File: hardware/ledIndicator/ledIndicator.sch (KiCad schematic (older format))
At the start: 12 parts

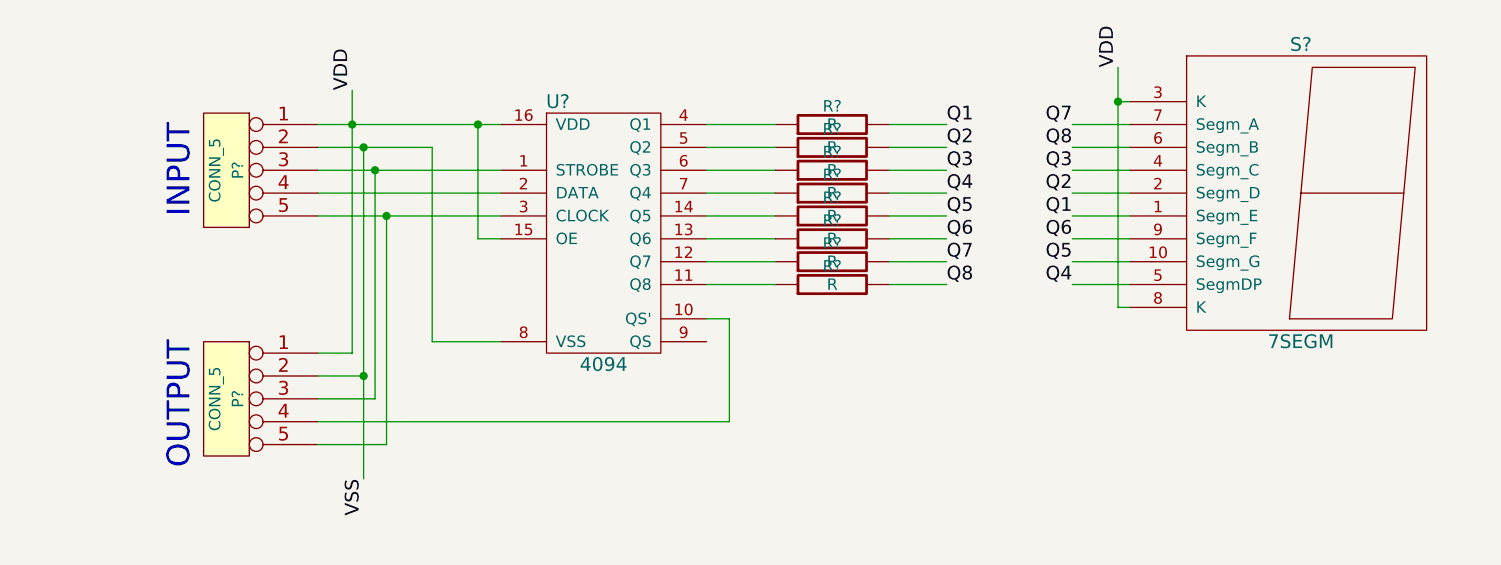
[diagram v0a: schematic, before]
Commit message: Initial design of the layout on pcb
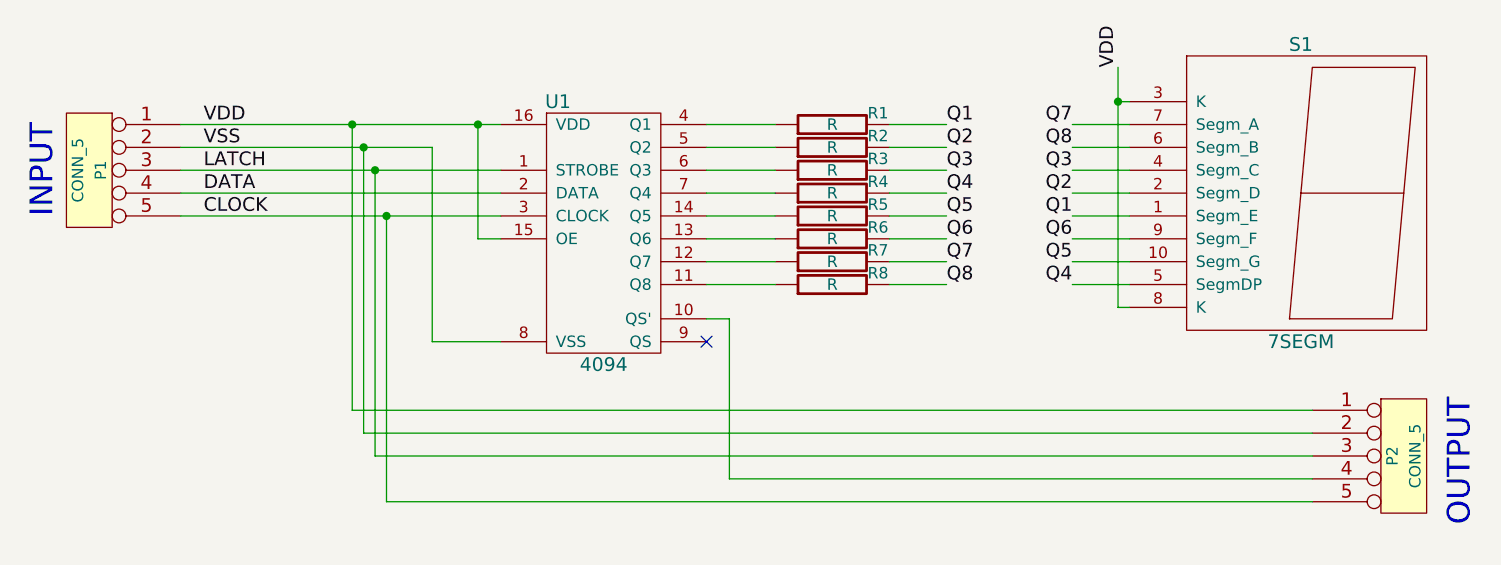
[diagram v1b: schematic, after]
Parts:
- P1, P2: renamed from P?; footprint (none) -> SMD_CONN5
- R1, R2, R3, R4, R5, R6, R7, R8: renamed from R?; footprint (none) -> SM0603_Resistor
- S1: renamed from S?; footprint (none) -> SA56
- U1: renamed from U?; footprint (none) -> SO16N
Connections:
- net LATCH: now reaches P1.3, P2.3, U1.1 (STROBE)
- net DATA: now reaches P1.4, U1.2 (DATA)
- net CLOCK: now reaches P1.5, P2.5, U1.3 (CLOCK)
- no-connect marks 0 -> 1
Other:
- moved on the sheet: P1, P2
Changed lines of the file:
@@
-EESchema Schematic File Version 2  date  3.01.2013 (чт)  1,24,30 EET
+EESchema Schematic File Version 2  date Thu 03 Jan 2013 05:14:04 PM EET
 LIBS:power
 LIBS:device
@@
 LIBS:contrib
 LIBS:valves
+LIBS:ledIndicator-cache
 EELAYER 27 0
 EELAYER END
@@
 Sheet 1 1
 Title "7 SEGMENT LED DISPLAY FOR PIPO"
-Date "2 jan 2013"
+Date "3 jan 2013"
 Rev "rev.A"
 Comp ""
@@
 $EndDescr
 $Comp
-L 7SEGM S?
+L 7SEGM S1
 U 1 1 50E4B02C
 P 7950 3450
-F 0 "S?" H 7950 4100 60  0000 C CNN
+F 0 "S1" H 7950 4100 60  0000 C CNN
 F 1 "7SEGM" H 7950 2800 60  0000 C CNN
+F 2 "SA56" H 7950 3450 60  0001 C CNN
 	1    7950 3450
 	1    0    0    -1
 $EndComp
 $Comp
-L 4094 U?
+L 4094 U1
 U 1 1 50E4C062
 P 4900 3700
-F 0 "U?" H 4700 4350 60  0000 C CNN
+F 0 "U1" H 4700 4350 60  0000 C CNN
 F 1 "4094" H 4900 3200 60  0000 C CNN
+F 2 "SO16N" H 4900 3700 60  0001 C CNN
 	1    4900 3700
 	1    0    0    -1
 $EndComp
 $Comp
-L R R?
+L R R1
 U 1 1 50E4C08F
 P 5900 3150
-F 0 "R?" V 5980 3150 50  0000 C CNN
+F 0 "R1" V 5950 2950 50  0000 C CNN
 F 1 "R" V 5900 3150 50  0000 C CNN
+F 2 "SM0603_Resistor" H 5900 3150 60  0001 C CNN
 	1    5900 3150
 	0    -1   -1   0
 $EndComp
 $Comp
-L R R?
+L R R2
 U 1 1 50E4C0AB
 P 5900 3250
-F 0 "R?" V 5980 3250 50  0000 C CNN
+F 0 "R2" V 5950 3050 50  0000 C CNN
 F 1 "R" V 5900 3250 50  0000 C CNN
+F 2 "SM0603_Resistor" H 5900 3250 60  0001 C CNN
 	1    5900 3250
 	0    -1   -1   0
 $EndComp
 $Comp
-L R R?
+L R R3
 U 1 1 50E4C0B1
 P 5900 3350
-F 0 "R?" V 5980 3350 50  0000 C CNN
+F 0 "R3" V 5950 3150 50  0000 C CNN
 F 1 "R" V 5900 3350 50  0000 C CNN
+F 2 "SM0603_Resistor" H 5900 3350 60  0001 C CNN
 	1    5900 3350
 	0    -1   -1   0
 $EndComp
 $Comp
-L R R?
+L R R4
 U 1 1 50E4C0B7
 P 5900 3450
-F 0 "R?" V 5980 3450 50  0000 C CNN
+F 0 "R4" V 5950 3250 50  0000 C CNN
 F 1 "R" V 5900 3450 50  0000 C CNN
+F 2 "SM0603_Resistor" H 5900 3450 60  0001 C CNN
 	1    5900 3450
 	0    -1   -1   0
 $EndComp
 $Comp
-L R R?
+L R R5
 U 1 1 50E4C0BD
 P 5900 3550
-F 0 "R?" V 5980 3550 50  0000 C CNN
+F 0 "R5" V 5950 3350 50  0000 C CNN
 F 1 "R" V 5900 3550 50  0000 C CNN
+F 2 "SM0603_Resistor" H 5900 3550 60  0001 C CNN
 	1    5900 3550
 	0    -1   -1   0
@@
 	5350 3550 5650 3550
 $Comp
-L R R?
+L R R6
 U 1 1 50E4C0DC
 P 5900 3650
-F 0 "R?" V 5980 3650 50  0000 C CNN
+F 0 "R6" V 5950 3450 50  0000 C CNN
 F 1 "R" V 5900 3650 50  0000 C CNN
+F 2 "SM0603_Resistor" H 5900 3650 60  0001 C CNN
 	1    5900 3650
 	0    -1   -1   0
 $EndComp
 $Comp
-L R R?
+L R R7
 U 1 1 50E4C0E2
 P 5900 3750
-F 0 "R?" V 5980 3750 50  0000 C CNN
+F 0 "R7" V 5950 3550 50  0000 C CNN
 F 1 "R" V 5900 3750 50  0000 C CNN
+F 2 "SM0603_Resistor" H 5900 3750 60  0001 C CNN
 	1    5900 3750
 	0    -1   -1   0
 $EndComp
 $Comp
-L R R?
+L R R8
 U 1 1 50E4C0E8
 P 5900 3850
-F 0 "R?" V 5980 3850 50  0000 C CNN
+F 0 "R8" V 5950 3650 50  0000 C CNN
 F 1 "R" V 5900 3850 50  0000 C CNN
+F 2 "SM0603_Resistor" H 5900 3850 60  0001 C CNN
 	1    5900 3850
 	0    -1   -1   0
@@
 Q5
 $Comp
-L CONN_5 P?
+L CONN_5 P1
 U 1 1 50E4C2BB
-P 3250 3350
-F 0 "P?" V 3200 3350 50  0000 C CNN
-F 1 "CONN_5" V 3300 3350 50  0000 C CNN
-	1    3250 3350
+P 2650 3350
+F 0 "P1" V 2600 3350 50  0000 C CNN
+F 1 "CONN_5" V 2700 3350 50  0000 C CNN
+F 2 "SMD_CONN5" H 2650 3350 60  0001 C CNN
+	1    2650 3350
 	-1   0    0    -1
 $EndComp
 Wire Wire Line
-	3650 3150 4450 3150
-Wire Wire Line
-	3650 3250 4150 3250
+	3050 3150 4450 3150
+Wire Wire Line
+	3050 3250 4150 3250
 Wire Wire Line
 	4150 3250 4150 4100
@@
 	4150 4100 4450 4100
 Wire Wire Line
-	3650 3350 4450 3350
-Wire Wire Line
-	3650 3450 4450 3450
-Wire Wire Line
-	3650 3550 4450 3550
+	3050 3350 4450 3350
+Wire Wire Line
+	3050 3450 4450 3450
+Wire Wire Line
+	3050 3550 4450 3550
 Wire Wire Line
 	4450 3650 4350 3650
@@
 	4350 3650 4350 3150
 Connection ~ 4350 3150
-Wire Wire Line
-	3800 3000 3800 4150
 Connection ~ 3800 3150
-Text Label 3800 3000 1    60   ~ 0
+Text Label 3150 3150 0    60   ~ 0
 VDD
-Text Label 3850 4700 3    60   ~ 0
+Text Label 3150 3250 0    60   ~ 0
 VSS
 $Comp
-L CONN_5 P?
+L CONN_5 P2
 U 1 1 50E4C3F1
-P 3250 4350
-F 0 "P?" V 3200 4350 50  0000 C CNN
-F 1 "CONN_5" V 3300 4350 50  0000 C CNN
-	1    3250 4350
-	-1   0    0    -1
-$EndComp
-Text Notes 3100 3150 3    100  ~ 0
+P 8400 4600
+F 0 "P2" V 8350 4600 50  0000 C CNN
+F 1 "CONN_5" V 8450 4600 50  0000 C CNN
+F 2 "SMD_CONN5" H 8400 4600 60  0001 C CNN
+	1    8400 4600
+	1    0    0    -1
+$EndComp
+Text Notes 2500 3150 3    100  ~ 0
 INPUT
-Text Notes 3100 4100 3    100  ~ 0
+Text Notes 8700 4350 3    100  ~ 0
 OUTPUT
-Wire Wire Line
-	3850 3250 3850 4700
-Wire Wire Line
-	3850 4250 3650 4250
 Connection ~ 3850 3250
-Connection ~ 3850 4250
-Wire Wire Line
-	3800 4150 3650 4150
-Wire Wire Line
-	3900 3350 3900 4350
-Wire Wire Line
-	3900 4350 3650 4350
+Wire Wire Line
+	3900 3350 3900 4600
 Connection ~ 3900 3350
 Wire Wire Line
-	3650 4450 5450 4450
-Wire Wire Line
-	5450 4450 5450 4000
+	5450 4000 5450 4700
 Wire Wire Line
 	5450 4000 5350 4000
 Wire Wire Line
-	3950 3550 3950 4550
-Wire Wire Line
-	3950 4550 3650 4550
+	3950 3550 3950 4800
 Connection ~ 3950 3550
+Wire Wire Line
+	3950 4800 8000 4800
+Wire Wire Line
+	5450 4700 8000 4700
+NoConn ~ 5350 4100
+Wire Wire Line
+	3900 4600 8000 4600
+Wire Wire Line
+	8000 4500 3850 4500
+Wire Wire Line
+	3800 4400 8000 4400
+Wire Wire Line
+	3800 3150 3800 4400
+Wire Wire Line
+	3850 4500 3850 3250
+Text Label 3150 3350 0    60   ~ 0
+LATCH
+Text Label 3150 3450 0    60   ~ 0
+DATA
+Text Label 3150 3550 0    60   ~ 0
+CLOCK
 $EndSCHEMATC
